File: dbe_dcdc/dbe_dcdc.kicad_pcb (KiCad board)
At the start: 2 copper layers, 150 x 50 mm, 42 parts, among them J1 PMBUS, M1 MountingHole_3.2mm_M3_Pad_Top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, M2 MountingHole_3.2mm_M3_Pad_Top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, Q1 MMBT3904, Q2 MMBT3904, U1 DBE0125V2NBC

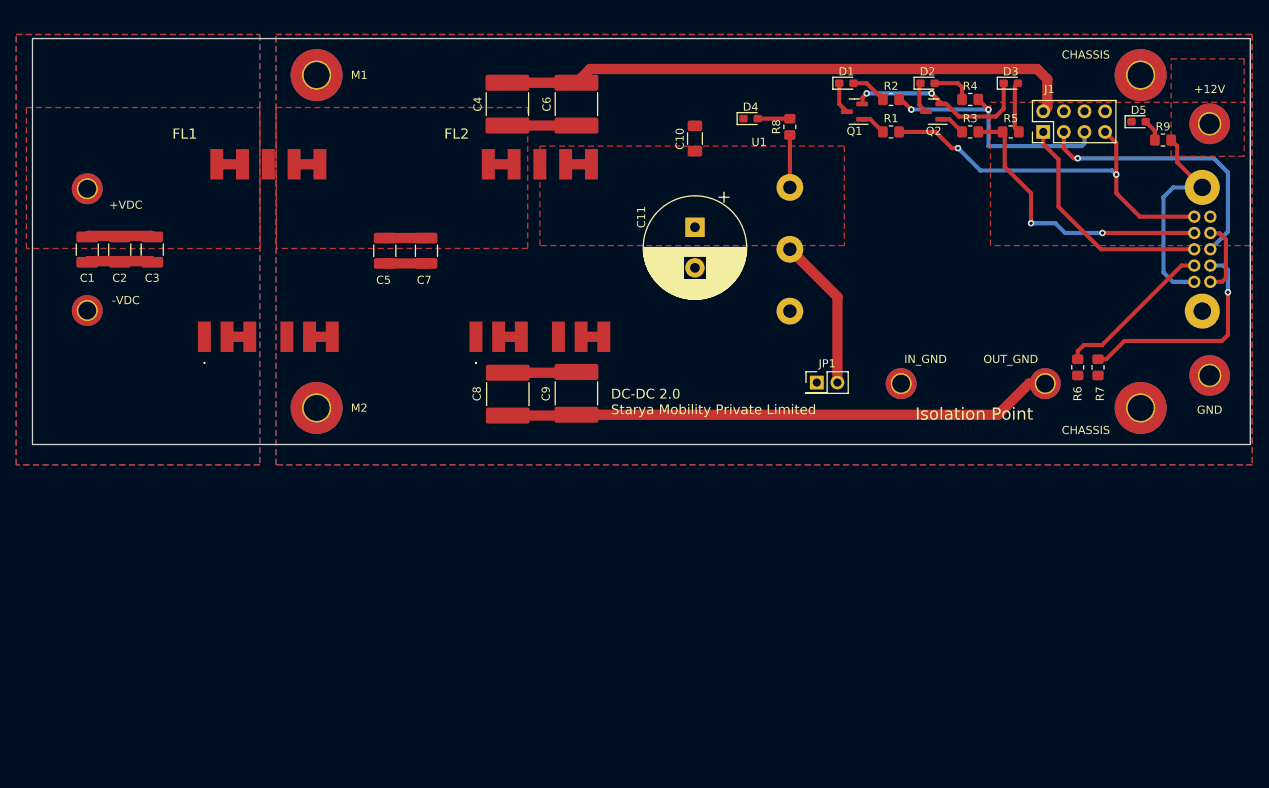
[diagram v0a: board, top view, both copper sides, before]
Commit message: layout and schema changes for out and in filtering
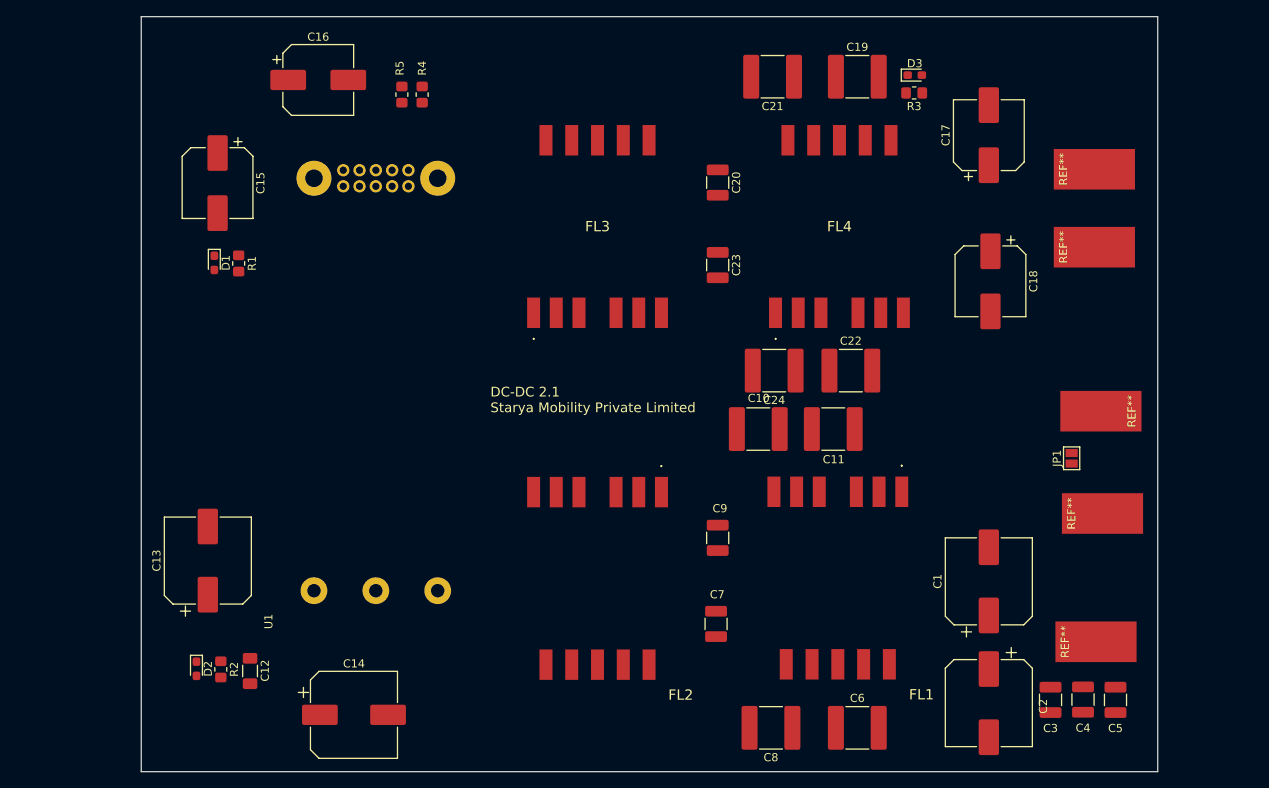
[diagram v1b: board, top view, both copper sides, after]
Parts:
- removed +12V, GND: MountingHole_2.5mm_Pad_TopBottom, MountingHole:MountingHole_2.5mm_Pad_TopBottom
- removed +VDC, -VDC, IN_GND, OUT_GND: MountingHole_2.2mm_M2_DIN965_Pad_TopBottom, MountingHole:MountingHole_2.2mm_M2_DIN965_Pad_TopBottom
- removed CHASSIS (x2), M1, M2: MountingHole_3.2mm_M3_Pad_TopBottom, MountingHole:MountingHole_3.2mm_M3_Pad_TopBottom
- removed the D1 at (120.2, 66.0)
- removed the D2 at (130.2, 66.0)
- removed J1: PMBUS, Connector_PinHeader_2.54mm:PinHeader_2x04_P2.54mm_Vertical
- removed Q1, Q2: MMBT3904, Package_TO_SOT_SMD:SOT-23
- removed the R1 at (125.8, 72.0)
- removed the R2 at (125.8, 68.0)
- removed the R3 at (135.5, 72.0)
- removed the R4 at (135.5, 68.0)
- added C1: 865080453014, Capacitor_SMD:CP_Elec_10x10.5, F.Cu at (137.8, 127.4)
- added C13: 865060857005, Capacitor_SMD:CP_Elec_10x10.5, F.Cu at (41.6, 124.8)
- added C15: 865080453014, Capacitor_SMD:CP_Elec_8x10.5, F.Cu at (42.8, 78.3)
- added C16: 865080453014, Capacitor_SMD:CP_Elec_8x10.5, F.Cu at (55.2, 65.6)
- added C17: 865080453014, Capacitor_SMD:CP_Elec_8x10.5, F.Cu at (137.8, 72.4)
- added C18: 865080453014, Capacitor_SMD:CP_Elec_8x10.5, F.Cu at (138.0, 90.4)
- added C19: GRM55DR72J224KW01L, Capacitor_SMD:C_2220_5650Metric_Pad1.97x5.40mm_HandSolder, F.Cu at (121.6, 65.2)
- added C2: 865060857005, Capacitor_SMD:CP_Elec_10x10.5, F.Cu at (137.8, 142.4)
- added C20: GRM32ER72A105KA01L, Capacitor_SMD:C_1210_3225Metric_Pad1.33x2.70mm_HandSolder, F.Cu at (104.4, 78.2)
- added C21: GRM55DR72J224KW01L, Capacitor_SMD:C_2220_5650Metric_Pad1.97x5.40mm_HandSolder, F.Cu at (111.2, 65.2)
- added C22: GRM55DR72J224KW01L, Capacitor_SMD:C_2220_5650Metric_Pad1.97x5.40mm_HandSolder, F.Cu at (120.8, 101.4)
- added C23: GRM32ER72A105KA01L, Capacitor_SMD:C_1210_3225Metric_Pad1.33x2.70mm_HandSolder, F.Cu at (104.4, 88.4)
- added C24: GRM55DR72J224KW01L, Capacitor_SMD:C_2220_5650Metric_Pad1.97x5.40mm_HandSolder, F.Cu at (111.4, 101.4)
- added FL3: PH9407.504NLT, PH9407_504NLT:PH9407_504NLT, F.Cu at (89.6, 83.4)
- added FL4: PH9407.504NLT, PH9407_504NLT:PH9407_504NLT, F.Cu at (119.4, 83.4)
- added REF**: SolderWirePad_1x01_SMD_5x10mm, Connector_Wire:SolderWirePad_1x01_SMD_5x10mm, F.Cu at (151.8, 119.0)
- added REF**: SolderWirePad_1x01_SMD_5x10mm, Connector_Wire:SolderWirePad_1x01_SMD_5x10mm, F.Cu at (150.8, 86.2)
- added REF**: SolderWirePad_1x01_SMD_5x10mm, Connector_Wire:SolderWirePad_1x01_SMD_5x10mm, F.Cu at (151.6, 106.4)
- added REF**: SolderWirePad_1x01_SMD_5x10mm, Connector_Wire:SolderWirePad_1x01_SMD_5x10mm, F.Cu at (151.0, 134.8)
- added REF**: SolderWirePad_1x01_SMD_5x10mm, Connector_Wire:SolderWirePad_1x01_SMD_5x10mm, F.Cu at (150.8, 76.6)
- C14: renamed from C11; value UHE2A221MHD -> 865060857005; footprint Capacitor_THT:CP_Radial_D12.5mm_P5.00mm -> Capacitor_SMD:CP_Elec_10x10.5
- JP1: footprint Connector_PinHeader_2.54mm:PinHeader_2x01_P2.54mm_Vertical -> Jumper:SolderJumper-2_P1.3mm_Open_Pad1.0x1.5mm
- moved C3 131.0 mm to (145.4, 142.0)
- moved C5 131.0 mm to (153.4, 142.0)
- moved C4 131.0 mm to (149.4, 141.9)
- moved D1 100.6 mm to (42.4, 88.1), turned to -90 degrees
- moved R2 96.8 mm to (43.2, 138.2), turned to -90 degrees
- moved R1 96.5 mm to (45.4, 88.2), turned to -90 degrees
- moved D2 96.2 mm to (40.2, 138.1), turned to -90 degrees
- moved R5 92.1 mm to (65.5, 67.4), turned to 90 degrees
- moved C6 88.1 mm to (121.6, 145.4), turned to 0 degrees
- moved R4 87.5 mm to (68.0, 67.4), turned to 90 degrees
- moved C12 85.5 mm to (46.8, 138.4), turned to -90 degrees
- moved U1 83.0 mm to (50.1, 133.1), turned to 90 degrees
- moved FL1 81.2 mm to (119.2, 127.2), turned to 180 degrees
- moved C8 80.5 mm to (111.0, 145.4), turned to 180 degrees
- moved C14 73.3 mm to (59.6, 143.8), turned to 0 degrees
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- renumbered C8 to C10, C9 to C11, C10 to C12, C1 to C3, C2 to C4, C3 to C5, C4 to C6, C5 to C7, C6 to C8, C7 to C9, D3 to D1, D4 to D2, D5 to D3, R5 to R1, R8 to R2, R9 to R3, R6 to R4, R7 to R5
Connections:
- C10 pad 2: GNDREF -> -VDC
- C11 pad 2: GNDREF -> -VDC
- C12 pad 2: GNDREF -> -VIN
- C14 pad 2: GNDREF -> -VIN
- C6 pad 2: GNDREF -> -VDC
- C8 pad 2: GNDREF -> -VDC
- D1 pad 1: GNDREF -> -VIN
- D2 pad 1: GNDREF -> -VIN
- D3 pad 1: GNDREF -> -VIN
- FL2 pad 5: GNDREF -> -VIN
- FL2 pad 6: GNDREF -> -VIN
- JP1 pad 1: GNDREF -> -VIN
- R4 pad 2: GNDREF -> -VIN
- R5 pad 2: GNDREF -> -VIN
- U1 pad 10: Net-(J1-Pad1) -> unconnected-(U1-Pad10)
- U1 pad 11: Net-(J1-Pad3) -> unconnected-(U1-Pad11)
- U1 pad 13: GNDREF -> -VIN
- U1 pad 14: SMB_ALERT -> unconnected-(U1-Pad14)
- U1 pad 16: +12V -> Net-(C15-Pad1)
- U1 pad 4: GNDREF -> -VIN
- U1 pad 5: GNDREF -> -VIN
- U1 pad 6: +12V -> Net-(C15-Pad1)
- U1 pad 7: GNDREF -> -VIN
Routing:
- net GNDREF: track 174.9 -> 0.00 mm, vias 2 -> 0
- net SMB_ALERT: track 47.8 -> 0.00 mm, vias 2 -> 0
- net P_GOOD: track 36.3 -> 0.00 mm, vias 2 -> 0
- net Net-(J1-Pad3): track 33.8 -> 0.00 mm, vias 1 -> 0
- net +3V3: track 31.2 -> 0.00 mm, vias 2 -> 0
- net Net-(J1-Pad1): track 28.9 -> 0.00 mm
- net Net-(R5-Pad1): track 27.6 -> 0.00 mm, vias 1 -> 0
- net +12V: track 26.3 -> 0.00 mm
- net Net-(C6-Pad1): track 20.0 -> 0.00 mm
- net Net-(R4-Pad1): track 19.7 -> 0.00 mm
- net Net-(C10-Pad1): track 19.2 -> 0.00 mm
- net ~{EN}: track 18.8 -> 0.00 mm
- net +VDC: track 11.3 -> 0.00 mm
- net -VDC: track 10.9 -> 0.00 mm
- net VIN: track 9.64 -> 0.00 mm
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- added copper zone on In1.Cu, net -VDC
- removed copper zone on F.Cu, net +12V
- removed copper zone on F.Cu, net +VDC
- removed copper zone on B.Cu, net -VDC
- removed copper zone on F.Cu, net -VDC
- removed copper zone on B.Cu, net GNDREF
- removed copper zone on F.Cu, net GNDREF
- removed copper zone on F.Cu, net Net-(C6-Pad1)
- removed copper zone on F.Cu, net VIN
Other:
- board size 150 x 50 mm -> 125.2 x 93 mm
- copper layers 2 -> 4
- board text added: "DC-DC 2.1 Starya Mobility Private Limited"
- board text removed: "DC-DC 2.0 Starya Mobility Private Limited"
- board text removed: "Isolation Point"
